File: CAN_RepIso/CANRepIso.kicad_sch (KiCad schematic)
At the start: 43 parts, among them J1 RBUS_IN, J2 RBUS_OUT, U6 SN65HVD230, U7 PLACEHOLDER ISOLATOR, U8 SN65HVD230

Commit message: Layout done
still needs touchups on the planes and the rounded corner
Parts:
- removed C6, C9: 160pF, Capacitor_SMD:C_0603_1608Metric, symbol Device:C_Small
- removed JP1: J_3.3, Jumper:SolderJumper-2_P1.3mm_Open_RoundedPad1.0x1.5mm, symbol Jumper:SolderJumper_2_Open
- removed JP2: J_GND, Jumper:SolderJumper-2_P1.3mm_Open_RoundedPad1.0x1.5mm, symbol Jumper:SolderJumper_2_Open
- removed R4, R5, R6, R7: 90, Resistor_SMD:R_0603_1608Metric, symbol Device:R_Small
- added TP10, TP7, TP8, TP9: TestPoint, TestPoint:TestPoint_Pad_D2.0mm, symbol Connector:TestPoint
- TP1, TP2, TP3, TP4, TP5, TP6: footprint TestPoint:TestPoint_Pad_1.5x1.5mm -> TestPoint:TestPoint_Pad_D1.5mm
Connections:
- net +3.3VA: now also TP9.1
- net +3V3: now also TP7.1
- net GND: now also TP8.1; no longer H3.1, H4.1
- net GND1: now also H3.1, H4.1, TP10.1
- net RX1: now also U6.4 (R)
- net TX1: now also U6.1 (D)
- net Vref: no longer C12.1, R10.1, R9.2, U8.5 (Vref)
- net at U8.1 (D): now also TP5.1, U7.6 (VOB)
- net at U8.4 (R): now also TP6.1, U7.7 (VIA)
- new net Vref2: C12.1, R10.1, R9.2, U8.5 (Vref)
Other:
- note added: "Bridge both of these with wires when the board is used as a repeater with no isolation"
- note removed: "Bridge both of these when the board is used as a repeater with no isolation"
- moved on the sheet: H1, H3, H4

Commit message: Added text and logos
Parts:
- renumbered J1 to RBUS1, J2 to RBUS2
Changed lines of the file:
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@@
   (symbol (lib_id "Connector:Conn_01x06_Female") (at 15.24 88.9 180) (unit 1)
     (in_bom yes) (on_board yes)
-    (property "Reference" "J1" (id 0) (at 16.51 74.93 0))
+    (property "Reference" "RBUS1" (id 0) (at 16.51 74.93 0))
     (property "Value" "RBUS_IN" (id 1) (at 16.51 77.4669 0))
     (property "Footprint" "Connector_Molex:Molex_Mini-Fit_Jr_5566-06A_2x03_P4.20mm_Vertical" (id 2) (at 15.24 88.9 0)
@@
   (symbol (lib_id "Connector:Conn_01x06_Female") (at 273.05 88.9 0) (unit 1)
     (in_bom yes) (on_board yes) (fields_autoplaced)
-    (property "Reference" "J2" (id 0) (at 273.7612 89.3353 0)
+    (property "Reference" "RBUS2" (id 0) (at 273.7612 89.3353 0)
       (effects (font (size 1.27 1.27)) (justify left))
     )
@@
       (reference "H4") (unit 1) (value "MountingHole_Pad") (footprint "MountingHole:MountingHole_3.2mm_M3_DIN965_Pad")
     )
-    (path "/c03374e9-87ea-401d-8ec8-f0596c74ecdf"
-      (reference "J1") (unit 1) (value "RBUS_IN") (footprint "Connector_Molex:Molex_Mini-Fit_Jr_5566-06A_2x03_P4.20mm_Vertical")
-    )
-    (path "/c2860ad5-8d7f-4d2b-b32e-981e245ea210"
-      (reference "J2") (unit 1) (value "RBUS_OUT") (footprint "Connector_Molex:Molex_Mini-Fit_Jr_5566-06A_2x03_P4.20mm_Vertical")
-    )
     (path "/8c5f9924-03c7-4523-a937-f68d2c72927e"
       (reference "R1") (unit 1) (value "60") (footprint "Resistor_SMD:R_0805_2012Metric")
@@
       (reference "R12") (unit 1) (value "4.42k") (footprint "Resistor_SMD:R_0603_1608Metric")
     )
+    (path "/c03374e9-87ea-401d-8ec8-f0596c74ecdf"
+      (reference "RBUS1") (unit 1) (value "RBUS_IN") (footprint "Connector_Molex:Molex_Mini-Fit_Jr_5566-06A_2x03_P4.20mm_Vertical")
+    )
+    (path "/c2860ad5-8d7f-4d2b-b32e-981e245ea210"
+      (reference "RBUS2") (unit 1) (value "RBUS_OUT") (footprint "Connector_Molex:Molex_Mini-Fit_Jr_5566-06A_2x03_P4.20mm_Vertical")
+    )
     (path "/7bfbc94b-8040-4dbe-92b6-07448d6dccf3"

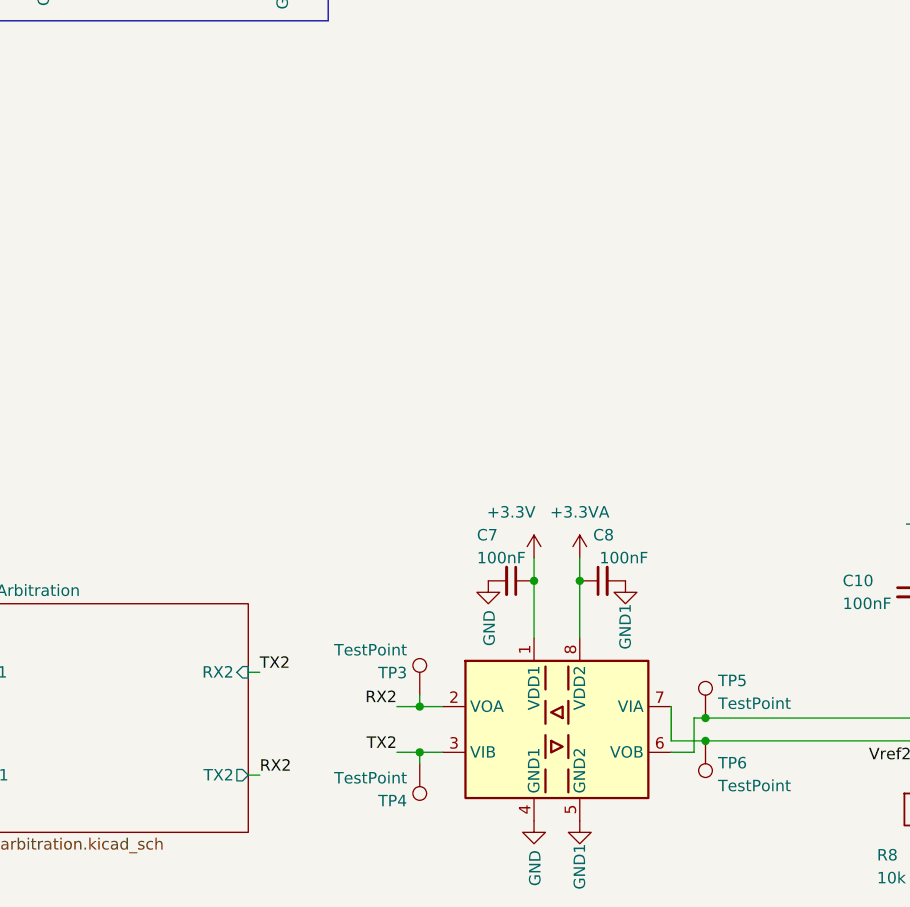
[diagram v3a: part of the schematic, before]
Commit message: added option for a 2nd digital isolator
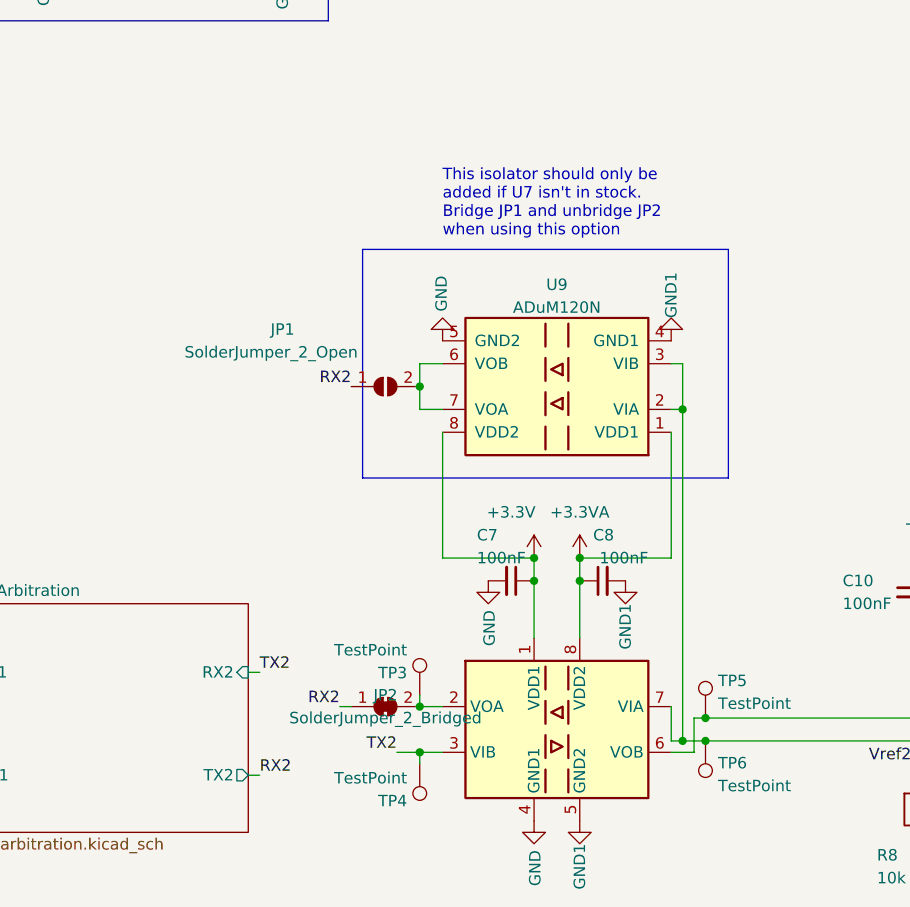
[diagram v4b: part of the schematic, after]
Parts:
- added JP1: SolderJumper_2_Open, Jumper:SolderJumper-2_P1.3mm_Open_RoundedPad1.0x1.5mm, symbol Jumper:SolderJumper_2_Open
- added JP2: SolderJumper_2_Bridged, Jumper:SolderJumper-2_P1.3mm_Bridged_RoundedPad1.0x1.5mm, symbol Jumper:SolderJumper_2_Bridged
- added U9: ADuM120N, Package_SO:SOIC-8_3.9x4.9mm_P1.27mm, symbol Isolator:ADuM120N
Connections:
- net +3.3VA: now also U9.1 (VDD1)
- net +3V3: now also U9.8 (VDD2)
- net GND: now also U9.5 (GND2)
- net GND1: now also U9.4 (GND1)
- net RX2: now also JP1.1 (A), JP2.1 (A); no longer TP3.1, U7.2 (VOA)
- net at TP6.1, U7.7 (VIA), U8.4 (R): now also U9.2 (VIA), U9.3 (VIB)
- new net: JP1.2 (B), U9.6 (VOB), U9.7 (VOA)
- new net: JP2.2 (B), TP3.1, U7.2 (VOA)
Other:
- note added: "This isolator should only be added if U7 isn't in stock. Bridge JP1 and unbridge JP2 when using this option"

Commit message: fixed schematic, layout needs update
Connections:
- net RX2: now also TP4.1, U7.3 (VIB); no longer JP2.1 (A)
- net TX2: now also JP2.1 (A); no longer TP4.1, U7.3 (VIB)

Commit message: v2 finished pre-review
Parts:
- added C22, C23: 2.2uF, Capacitor_SMD:C_0402_1005Metric, symbol Device:C_Small
- added C6, C9: 1pF, Capacitor_SMD:C_0402_1005Metric, symbol Device:C_Small
- added D3: RX1LED, LED_SMD:LED_0402_1005Metric, symbol Device:LED_Small
- added D4: TX1LED, LED_SMD:LED_0402_1005Metric, symbol Device:LED_Small
- added D5: RX2LED, LED_SMD:LED_0402_1005Metric, symbol Device:LED_Small
- added D6: TX2LED, LED_SMD:LED_0402_1005Metric, symbol Device:LED_Small
- added D7: 3V31LED, LED_SMD:LED_0402_1005Metric, symbol Device:LED_Small
- added D8: 3V32LED, LED_SMD:LED_0402_1005Metric, symbol Device:LED_Small
- added JP3, JP4: SolderJumper_2_Bridged, Jumper:SolderJumper-2_P1.3mm_Bridged_RoundedPad1.0x1.5mm, symbol Jumper:SolderJumper_2_Bridged
- added R13, R14: 470, Resistor_SMD:R_0402_1005Metric, symbol Device:R_Small
- added R15, R16: 0, Resistor_SMD:R_0402_1005Metric, symbol Device:R_Small
- added R4, R5, R6, R7: 1k, Resistor_SMD:R_0402_1005Metric, symbol Device:R_Small
- added TP11, TP12: TestPoint, Connector_PinHeader_2.54mm:PinHeader_1x01_P2.54mm_Vertical, symbol Connector:TestPoint
- added U10, U11: AP2205-33W5-7, iclr:SOT95P282X145-5N, symbol iclr:AP2205-W5-7
- C1: value 220 pF -> 1pF; footprint Capacitor_SMD:C_0603_1608Metric -> Capacitor_SMD:C_0402_1005Metric
- C10, C11, C4, C5, C7, C8: footprint Capacitor_SMD:C_0603_1608Metric -> Capacitor_SMD:C_0402_1005Metric
- C12, C3: value 0.1uF -> 47nF; footprint Capacitor_SMD:C_0603_1608Metric -> Capacitor_SMD:C_0402_1005Metric
- C13: value 220pF -> 1uF; footprint Capacitor_SMD:C_0603_1608Metric -> Capacitor_SMD:C_0402_1005Metric
- C14: value 220 pF -> 1uF; footprint Capacitor_SMD:C_0603_1608Metric -> Capacitor_SMD:C_0402_1005Metric
- C2: value 220pF -> 1pF; footprint Capacitor_SMD:C_0603_1608Metric -> Capacitor_SMD:C_0402_1005Metric
- R1, R10, R2, R9: footprint Resistor_SMD:R_0805_2012Metric -> Resistor_SMD:R_0603_1608Metric
- R3, R8: value 10k -> 0
- RBUS1, RBUS2: footprint Connector_Molex:Molex_Mini-Fit_Jr_5566-06A_2x03_P4.20mm_Vertical -> Connector_Molex:Molex_Mini-Fit_Jr_5569-06A2_2x03_P4.20mm_Horizontal
- TP1, TP2, TP3, TP4, TP5, TP6: footprint TestPoint:TestPoint_Pad_D1.5mm -> TestPoint:TestPoint_Pad_D1.0mm
- TP10, TP7, TP8, TP9: footprint TestPoint:TestPoint_Pad_D2.0mm -> Connector_PinHeader_2.54mm:PinHeader_1x01_P2.54mm_Vertical
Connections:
- net +3.3VA: now also C22.1, JP3.1 (A), R14.1, R6.1, R7.1, U11.5 (VOUT); no longer RBUS2.3 (Pin_3)
- net +3V3: now also C23.1, JP4.2 (B), R13.1, R4.1, R5.1, U10.5 (VOUT); no longer RBUS1.3 (Pin_3)
- net GND: now also C1.2, C13.2, C2.2, C23.2, D7.1 (K), U10.2 (GND); no longer C1.1, C2.1
- net GND1: now also C14.2, C22.2, C6.2, C9.2, D8.1 (K), U11.2 (GND); no longer C13.1, C14.1
- net RX1: now also C1.1, D3.1 (K)
- net RX2: no longer JP1.1 (A)
- net TX1: now also C2.1, D4.1 (K)
- net TX2: now also JP1.1 (A)
- net Vref: now also R15.2; no longer U6.5 (Vref)
- net Vref2: now also R16.1; no longer U8.5 (Vref)
- net TX2_PRE_ISO: now reaches TP5.1, U7.6 (VOB), U8.1 (D)
- net TX2_PRE_ISO: now also C9.1, D6.1 (K)
- net RX2_PRE_ISO: now reaches TP6.1, U7.7 (VIA), U8.4 (R), U9.2 (VIA), U9.3 (VIB)
- net RX2_PRE_ISO: now also C6.1, D5.1 (K)
- net Deploy1: now reaches RBUS1.4 (Pin_4)
- net Deploy1: now also TP11.1
- net Deploy2: now reaches RBUS2.4 (Pin_4)
- net Deploy2: now also TP12.1
- net CAN_HIGH_IN renamed CAN_IN_+
- net CAN_IN_+: no longer C2.2
- net CAN_HIGH_OUT renamed CAN_OUT_+
- net CAN_OUT_+: no longer C13.2
- net CAN_LOW_IN renamed CAN_IN_-
- net CAN_IN_-: no longer C1.2
- net CAN_LOW_OUT renamed CAN_OUT_-
- net CAN_OUT_-: no longer C14.2
- new net: D8.2 (A), R14.2
- new net: D3.2 (A), R4.2
- new net: R15.1, U6.5 (Vref)
- new net: D7.2 (A), R13.2
- new net: D4.2 (A), R5.2
- new net: R16.2, U8.5 (Vref)
- new net: D5.2 (A), R6.2
- new net: D6.2 (A), R7.2
- new net RBUS_uC_V1: C13.1, JP4.1 (A), RBUS1.3 (Pin_3), U10.1 (VIN), U10.3 (EN)
- new net RBUS_uC_V2: C14.1, JP3.2 (B), RBUS2.3 (Pin_3), U11.1 (VIN), U11.3 (EN)
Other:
- note added: "Don't bridge these if high current will be passing through"
- note added: "Tiny filter caps to remove overshoot"
- company: (none) -> ICLR
- title: (none) -> CAN Repeater and Isolator
- moved on the sheet: H3, H4, JP2, R3, TP10, TP7, TP8, TP9

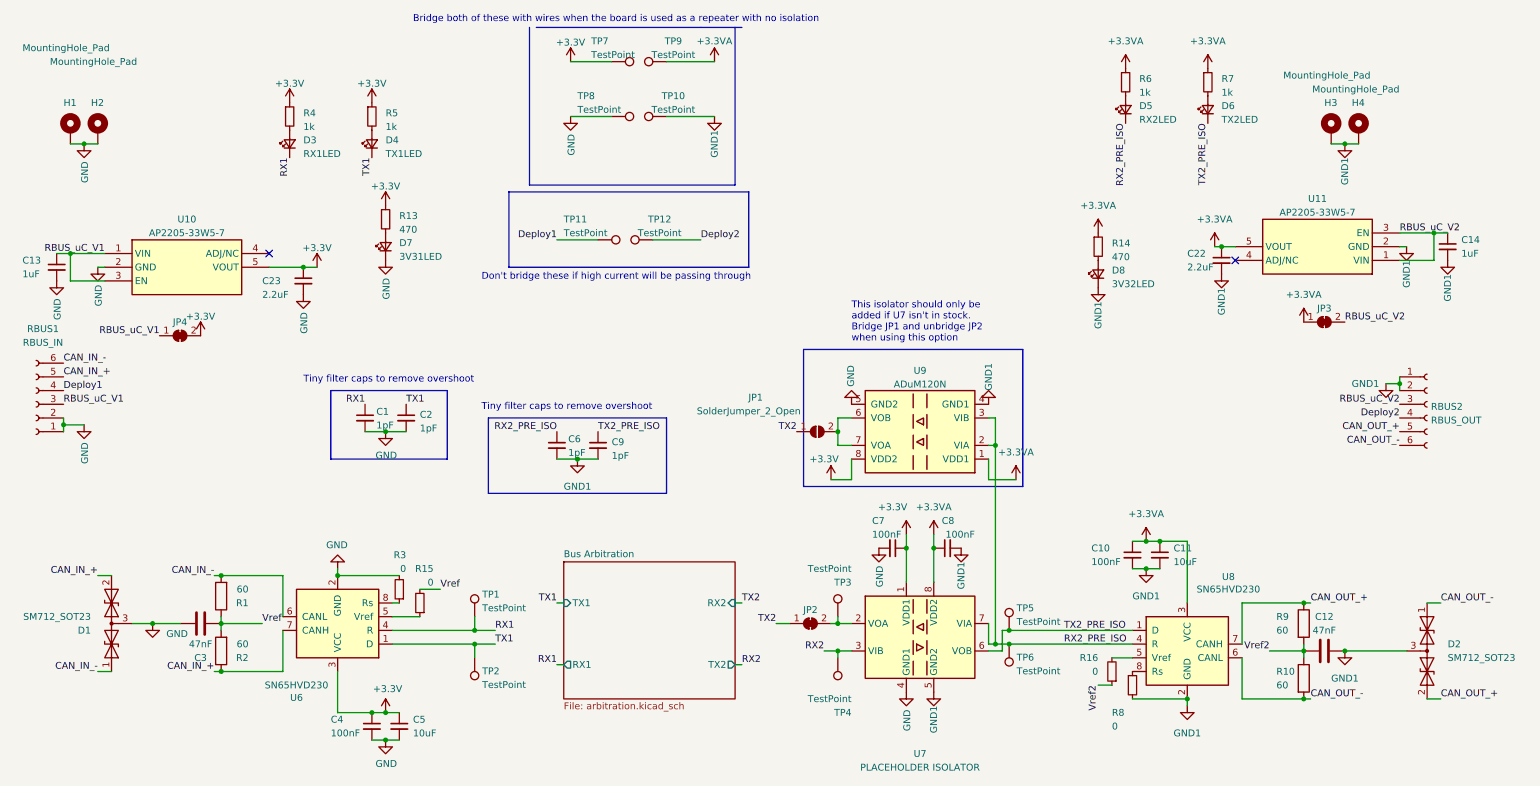
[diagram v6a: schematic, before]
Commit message: clean up schematic and bom
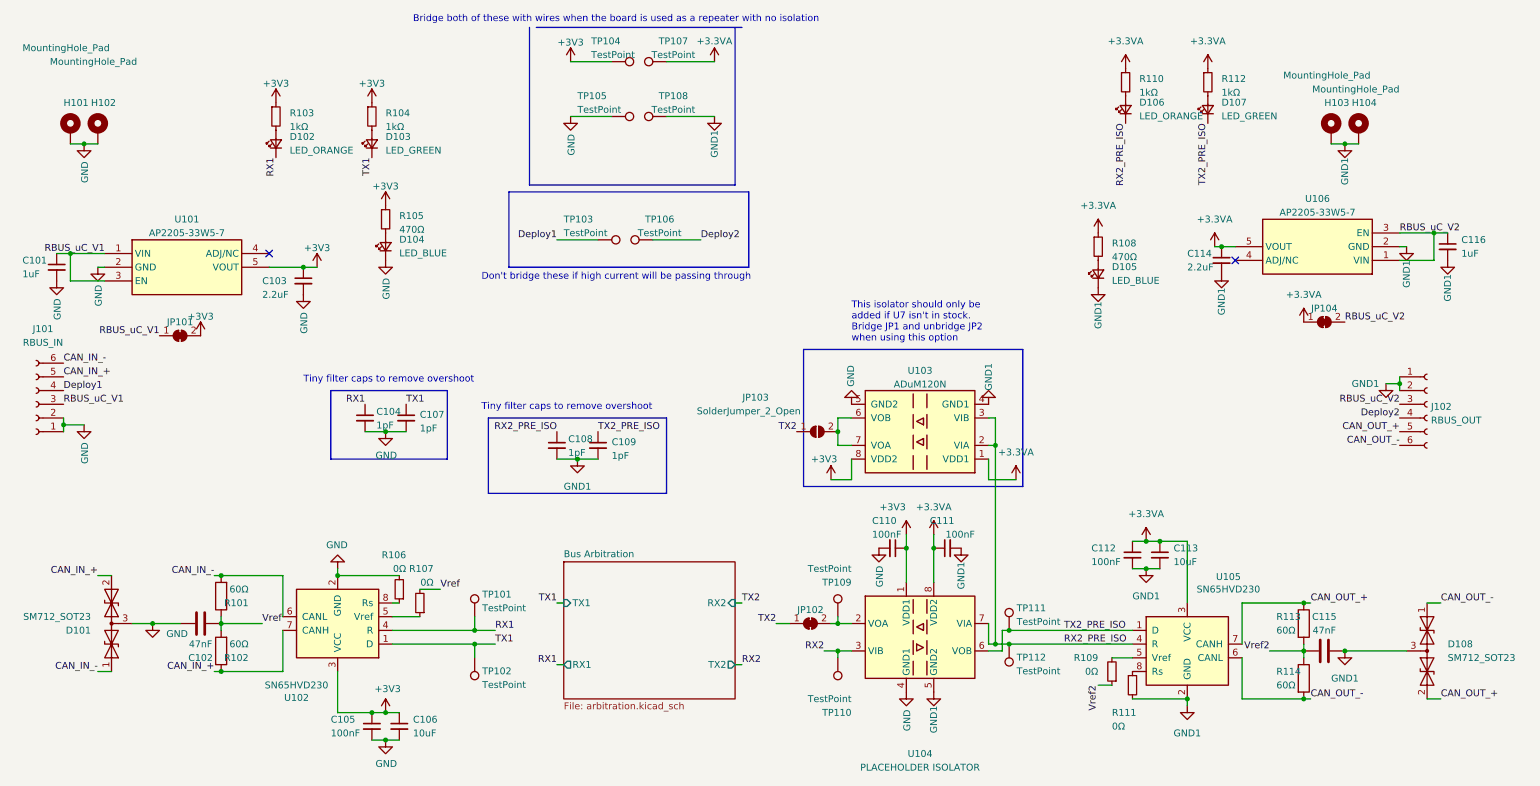
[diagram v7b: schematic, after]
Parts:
- D102: renamed from D3; value RX1LED -> LED_ORANGE
- D103: renamed from D4; value TX1LED -> LED_GREEN
- D104: renamed from D7; value 3V31LED -> LED_BLUE
- D105: renamed from D8; value 3V32LED -> LED_BLUE
- D106: renamed from D5; value RX2LED -> LED_ORANGE
- D107: renamed from D6; value TX2LED -> LED_GREEN
- H101: renamed from H1; now left out of the parts list
- H102: renamed from H2; now left out of the parts list
- H103: renamed from H3; now left out of the parts list
- H104: renamed from H4; now left out of the parts list
- JP101: renamed from JP4; now left out of the parts list
- JP102: renamed from JP2; now left out of the parts list
- JP103: renamed from JP1; now left out of the parts list
- JP104: renamed from JP3; now left out of the parts list
- R101: renamed from R1; value 60 -> 60Ω
- R102: renamed from R2; value 60 -> 60Ω
- R103: renamed from R4; value 1k -> 1kΩ
- R104: renamed from R5; value 1k -> 1kΩ
- R105: renamed from R13; value 470 -> 470Ω
- R106: renamed from R3; value 0 -> 0Ω
- R107: renamed from R15; value 0 -> 0Ω
- R108: renamed from R14; value 470 -> 470Ω
- R109: renamed from R16; value 0 -> 0Ω
- R110: renamed from R6; value 1k -> 1kΩ
- R111: renamed from R8; value 0 -> 0Ω
- R112: renamed from R7; value 1k -> 1kΩ
- R113: renamed from R9; value 60 -> 60Ω
- R114: renamed from R10; value 60 -> 60Ω
- TP101: renamed from TP1; now left out of the parts list
- TP102: renamed from TP2; now left out of the parts list
- TP103: renamed from TP11; now left out of the parts list
- TP104: renamed from TP7; now left out of the parts list
- TP105: renamed from TP8; now left out of the parts list
- TP106: renamed from TP12; now left out of the parts list
- TP107: renamed from TP9; now left out of the parts list
- TP108: renamed from TP10; now left out of the parts list
- TP109: renamed from TP3; now left out of the parts list
- TP110: renamed from TP4; now left out of the parts list
- TP111: renamed from TP5; now left out of the parts list
- TP112: renamed from TP6; now left out of the parts list
- renumbered C13 to C101, C3 to C102, C23 to C103, C1 to C104, C4 to C105, C5 to C106, C2 to C107, C6 to C108, C9 to C109, C7 to C110, C8 to C111, C10 to C112, C11 to C113, C22 to C114, C12 to C115, C14 to C116, D1 to D101, D2 to D108, RBUS1 to J101, RBUS2 to J102, U10 to U101, U6 to U102, U9 to U103, U7 to U104, U8 to U105, U11 to U106
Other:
- moved on the sheet: D102, R103
